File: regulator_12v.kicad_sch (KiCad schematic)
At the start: 16 parts, among them U4 MAX25240AFFD/VY+

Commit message: parts
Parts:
- C19, C20, C22: footprint Capacitor_SMD:C_0603_1608Metric -> Capacitor_SMD:C_0402_1005Metric
- C23, C25, C26, C27, C31: footprint Capacitor_SMD:C_1206_3216Metric -> Capacitor_SMD:C_0402_1005Metric
- C28, C29: footprint Capacitor_SMD:C_0805_2012Metric -> Capacitor_SMD:C_0402_1005Metric
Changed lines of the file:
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@@
 			)
 		)
-		(property "Footprint" "Capacitor_SMD:C_0603_1608Metric"
+		(property "Footprint" "Capacitor_SMD:C_0402_1005Metric"
 			(at 87.3252 90.17 0)
 			(effects
@@
 			)
 		)
-		(property "Footprint" "Capacitor_SMD:C_1206_3216Metric"
+		(property "Footprint" "Capacitor_SMD:C_0402_1005Metric"
 			(at 147.0152 132.08 0)
 			(effects
@@
 			)
 		)
-		(property "Footprint" "Capacitor_SMD:C_1206_3216Metric"
+		(property "Footprint" "Capacitor_SMD:C_0402_1005Metric"
 			(at 122.8852 132.08 0)
 			(effects
@@
 			)
 		)
-		(property "Footprint" "Capacitor_SMD:C_1206_3216Metric"
+		(property "Footprint" "Capacitor_SMD:C_0402_1005Metric"
 			(at 158.4452 132.08 0)
 			(effects
@@
 			)
 		)
-		(property "Footprint" "Capacitor_SMD:C_1206_3216Metric"
+		(property "Footprint" "Capacitor_SMD:C_0402_1005Metric"
 			(at 218.1352 91.44 0)
 			(effects
@@
 			)
 		)
-		(property "Footprint" "Capacitor_SMD:C_1206_3216Metric"
+		(property "Footprint" "Capacitor_SMD:C_0402_1005Metric"
 			(at 135.5852 132.08 0)
 			(effects
@@
 			)
 		)
-		(property "Footprint" "Capacitor_SMD:C_0603_1608Metric"
+		(property "Footprint" "Capacitor_SMD:C_0402_1005Metric"
 			(at 87.3252 110.49 0)
 			(effects
@@
 			)
 		)
-		(property "Footprint" "Capacitor_SMD:C_0805_2012Metric"
+		(property "Footprint" "Capacitor_SMD:C_0402_1005Metric"
 			(at 105.1052 90.17 0)
 			(effects
@@
 			)
 		)
-		(property "Footprint" "Capacitor_SMD:C_0603_1608Metric"
+		(property "Footprint" "Capacitor_SMD:C_0402_1005Metric"
 			(at 187.6552 114.3 0)
 			(effects
@@
 			)
 		)
-		(property "Footprint" "Capacitor_SMD:C_0805_2012Metric"
+		(property "Footprint" "Capacitor_SMD:C_0402_1005Metric"
 			(at 98.7552 90.17 0)
 			(effects

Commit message: part numebrs
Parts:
- C19, C20: LCSC (none) -> C307331
- C21: LCSC (none) -> C32949
- C22: LCSC (none) -> C84704
- C23: footprint Capacitor_SMD:C_0402_1005Metric -> Capacitor_SMD:C_0603_1608Metric; LCSC (none) -> C69335
- C25, C26, C27: footprint Capacitor_SMD:C_0402_1005Metric -> Capacitor_SMD:C_0805_2012Metric; LCSC (none) -> C602037
- C28, C29: footprint Capacitor_SMD:C_0402_1005Metric -> Capacitor_SMD:C_0603_1608Metric; LCSC (none) -> C96446
- C31: footprint Capacitor_SMD:C_0402_1005Metric -> Capacitor_SMD:C_1206_3216Metric; LCSC (none) -> C403725

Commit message: added schematics and footprints to project
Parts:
- U4: footprint International_Footprints:21-100399_90-100137_ADI -> Dry_Lettuce:MAX25240; symbol MAX25240:MAX25240AFFD_VY+ -> Dry_Lettuce:MAX25240AFFD_VY+
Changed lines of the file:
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@@
 	)
 	(symbol
-		(lib_id "MAX25240:MAX25240AFFD_VY+")
+		(lib_id "Dry_Lettuce:MAX25240AFFD_VY+")
 		(at 110.49 80.01 0)
 		(unit 1)
@@
 			)
 		)
-		(property "Footprint" "International_Footprints:21-100399_90-100137_ADI"
+		(property "Footprint" "Dry_Lettuce:MAX25240"
 			(at 110.49 80.01 0)
 			(effects

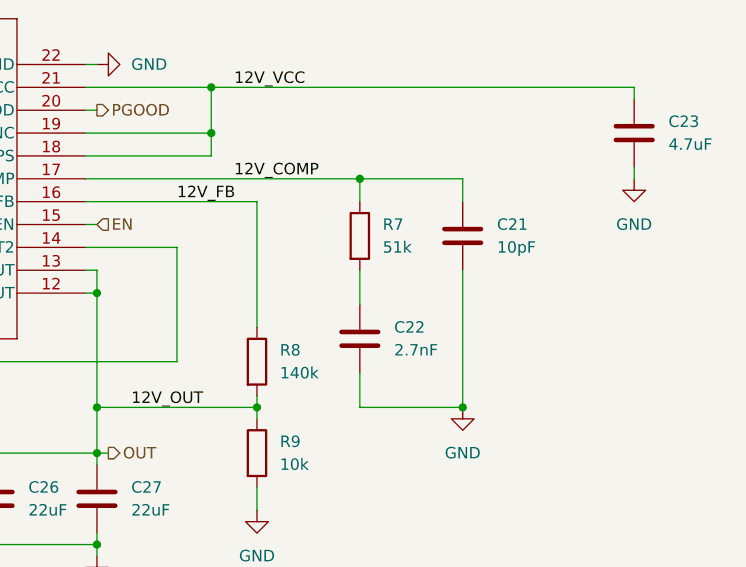
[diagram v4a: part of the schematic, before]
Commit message: added labels to everything
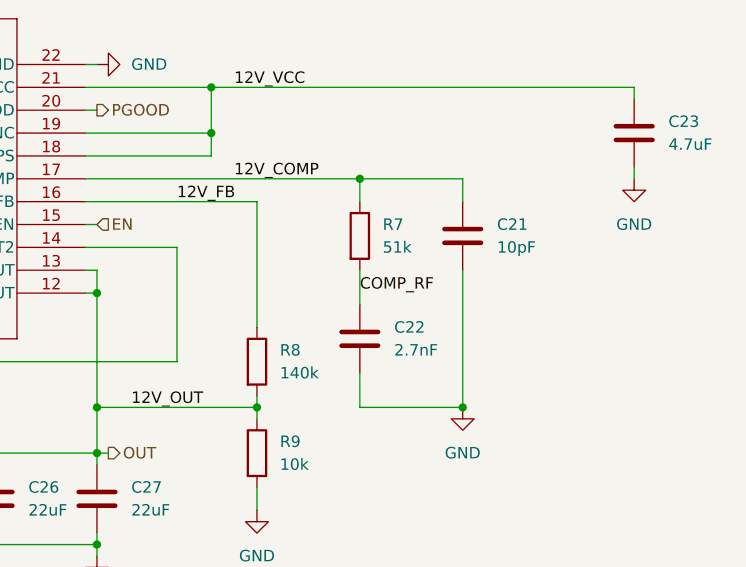
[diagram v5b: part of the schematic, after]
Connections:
- net COMP_RF: now reaches C22.1, R7.2
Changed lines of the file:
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@@
+		)
+	)
+	(label "COMP_RF"
+		(at 186.69 105.41 0)
+		(effects
+			(font
+				(size 1.27 1.27)
+			)
+			(justify left bottom)
 		)
 	)

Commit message: added some lcsc part ids
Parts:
- L1: LCSC (none) -> C3911470
- U4: LCSC (none) -> C18170722
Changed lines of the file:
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@@
 			)
 		)
-		(property "LCSC" ""
+		(property "LCSC" "C3911470"
 			(at 86.36 96.52 0)
 			(effects
@@
 			)
 		)
-		(property "LCSC" ""
+		(property "LCSC" "C18170722"
 			(at 110.49 80.01 0)
 			(effects
